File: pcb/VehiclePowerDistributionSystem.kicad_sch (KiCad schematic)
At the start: 28 parts, among them J1 B2B-XH-A, J2 B2B-XH-A, J3 B2B-XH-A, J4 B4B-XH-A, J5 B4B-XH-A, J6 B4B-XH-A, J7 B8B-XH-A, J8 FFC2B28-24-G, U1 TPS22810DRV, U2 D24V7F5, U3 D24V7F3, U7 TPS22810DRV

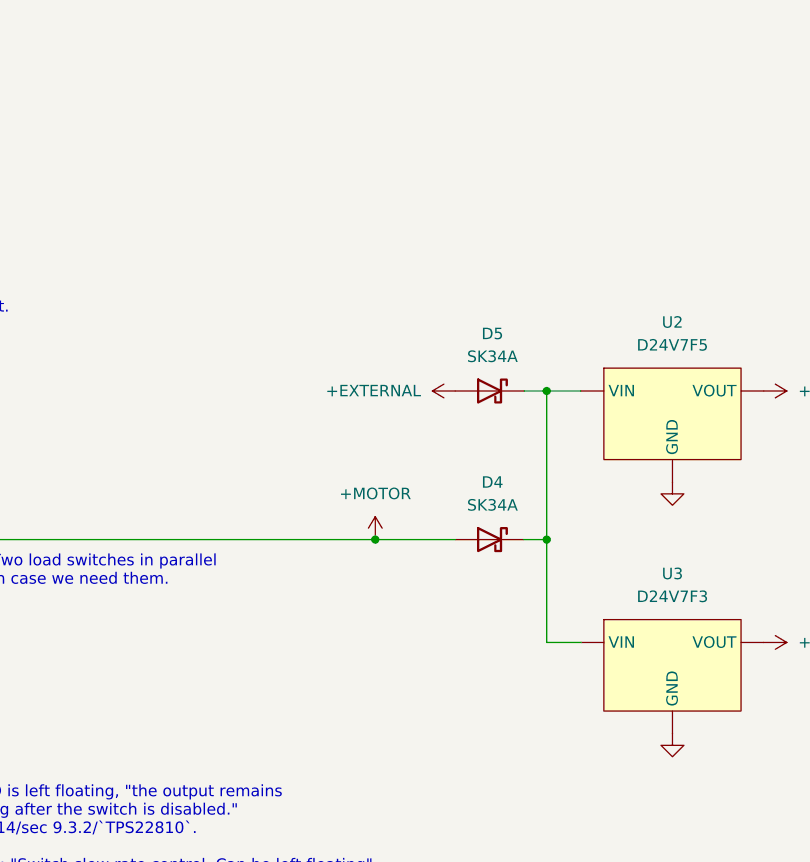
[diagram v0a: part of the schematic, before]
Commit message: Added LEDs for controlled battery and external power for `VehiclePowerDistributionSystem`.
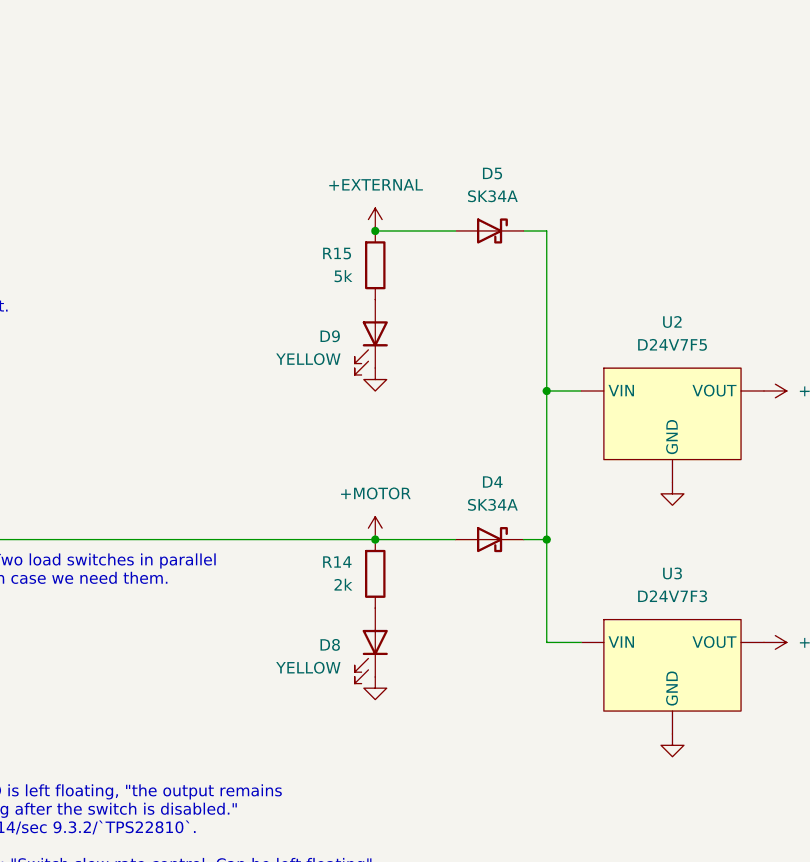
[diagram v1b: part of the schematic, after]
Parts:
- added D8, D9: YELLOW, LED_SMD:LED_1206_3216Metric_Pad1.42x1.75mm_HandSolder, symbol Device:LED
- added R14: 2k, Resistor_SMD:R_1206_3216Metric_Pad1.30x1.75mm_HandSolder, symbol Device:R
- added R15: 5k, Resistor_SMD:R_1206_3216Metric_Pad1.30x1.75mm_HandSolder, symbol Device:R
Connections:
- net +EXTERNAL: now also R15.2
- net +MOTOR: now also R14.2
- net GND: now also D8.1 (K), D9.1 (K)
- new net: D8.2 (A), R14.1
- new net: D9.2 (A), R15.1
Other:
- moved on the sheet: D5

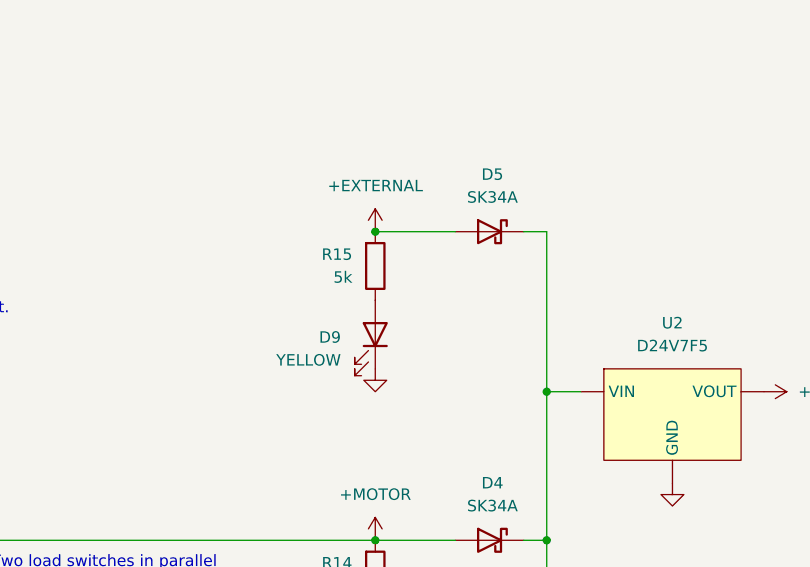
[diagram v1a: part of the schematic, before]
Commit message: Added more silkscreen text for `VehiclePowerDistributionSystem`.
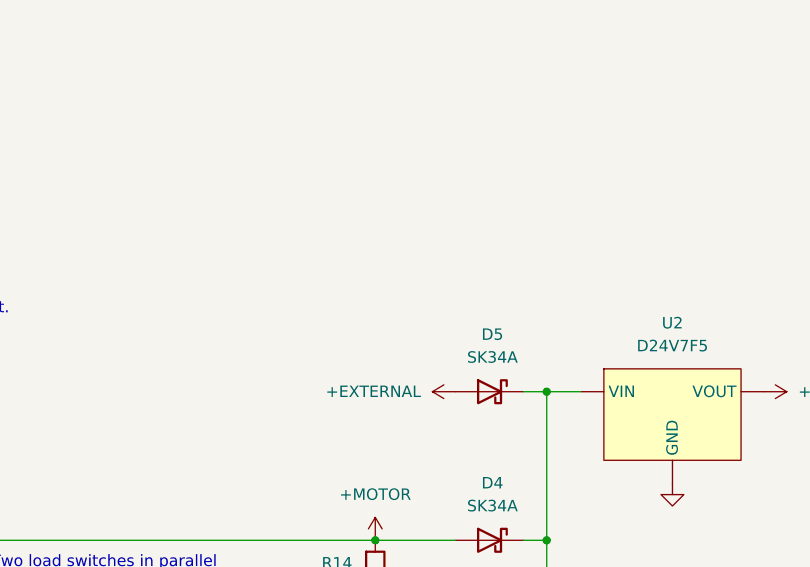
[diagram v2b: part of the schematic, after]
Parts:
- removed D9: YELLOW, LED_SMD:LED_1206_3216Metric_Pad1.42x1.75mm_HandSolder, symbol Device:LED
- removed R15: 5k, Resistor_SMD:R_1206_3216Metric_Pad1.30x1.75mm_HandSolder, symbol Device:R
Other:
- moved on the sheet: D5

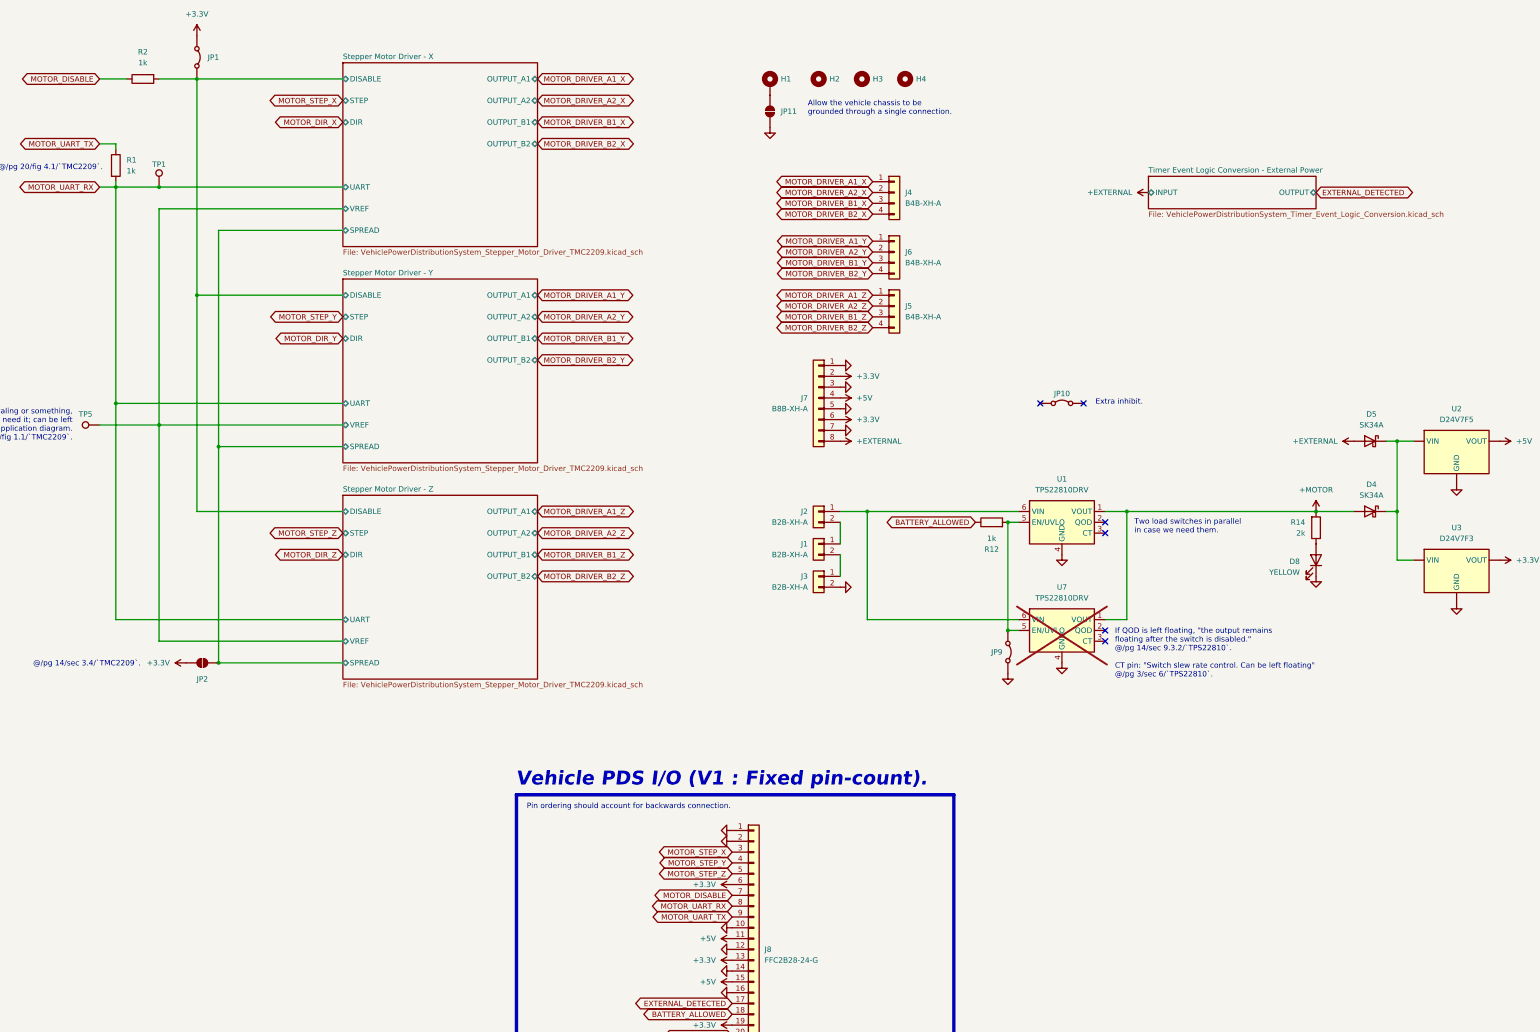
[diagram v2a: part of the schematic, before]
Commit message: Geographically reannotated `VehiclePowerDistributionSystem`.
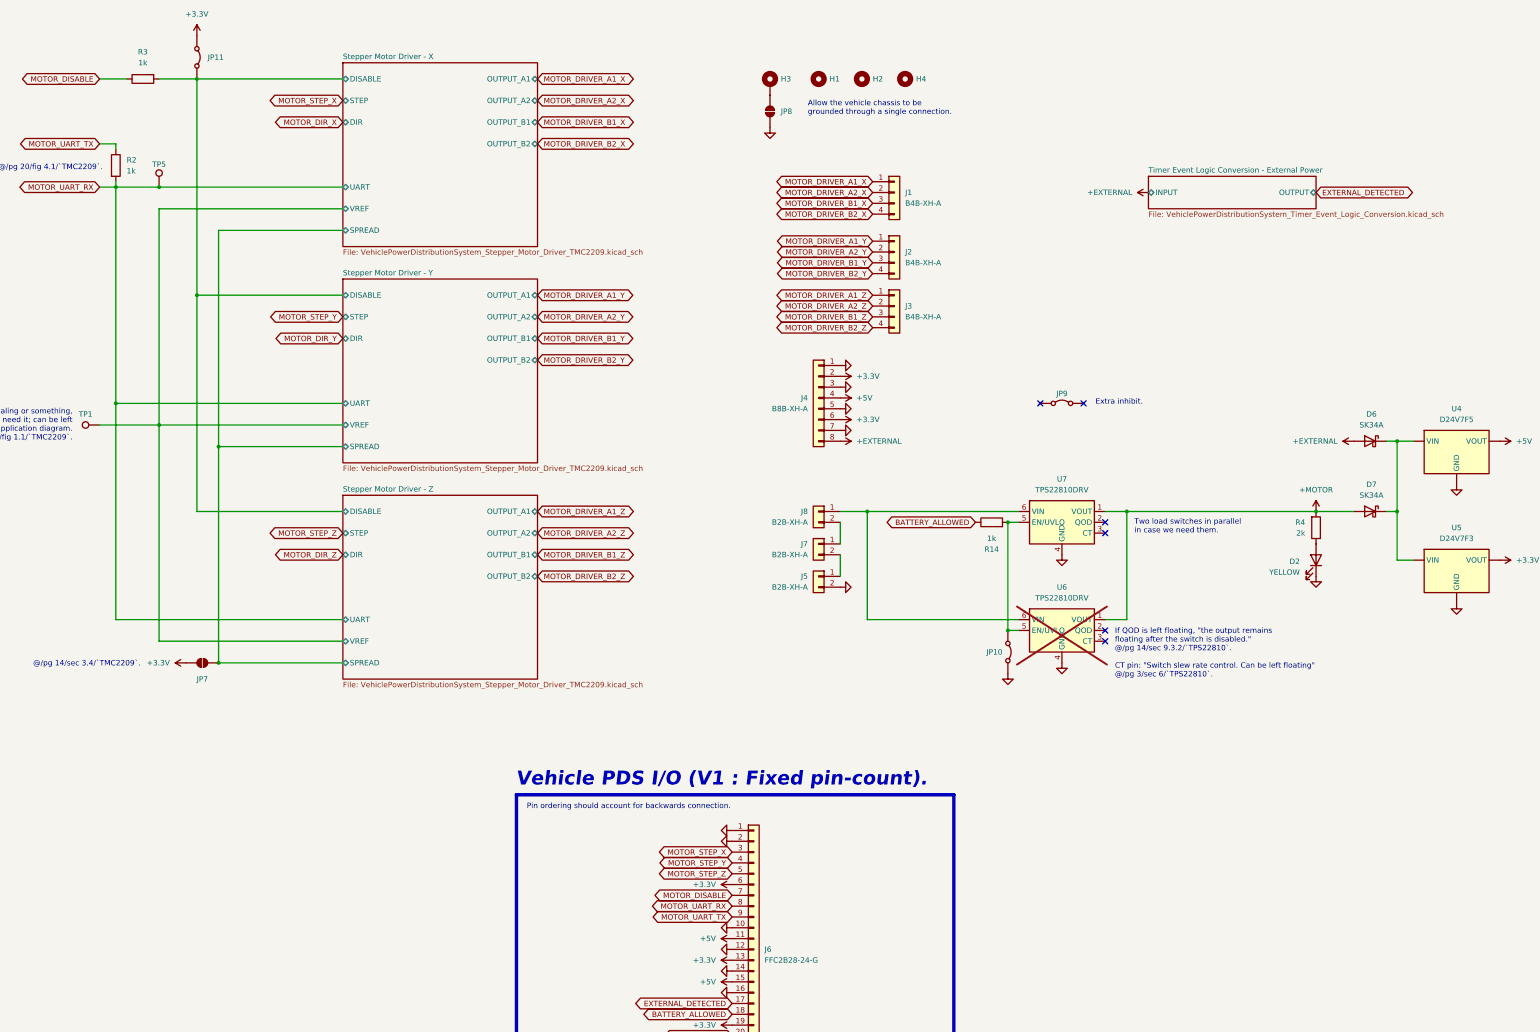
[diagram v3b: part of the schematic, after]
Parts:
- J6: renamed from J8; DigiKey (none) -> https://www.digikey.com/en/products/detail/gct/FFC2B28-24-G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
- renumbered D8 to D2, D5 to D6, D4 to D7, H2 to H1, H3 to H2, H1 to H3, J4 to J1, J6 to J2, J5 to J3, J7 to J4, J3 to J5, J1 to J7, J2 to J8, JP9 to JP10, JP1 to JP11, JP2 to JP7, JP11 to JP8, JP10 to JP9, R12 to R14, R1 to R2, R2 to R3, R14 to R4, TP5 to TP1, TP1 to TP5, U2 to U4, U3 to U5, U7 to U6, U1 to U7
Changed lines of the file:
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@@
 		(on_board yes)
 		(dnp no)
-		(property "Reference" "TP1"
+		(property "Reference" "TP5"
 			(at 81.28 58.166 0)
 			(effects
@@
 			(project "VehiclePowerDistributionSystem"
 				(path "/92a7a41c-8494-4e4b-ac2d-deb1f1cd8085"
-					(reference "TP1")
+					(reference "TP5")
 					(unit 1)
 				)
@@
 		(on_board yes)
 		(dnp no)
-		(property "Reference" "R12"
+		(property "Reference" "R14"
 			(at 276.86 148.59 90)
 			(effects
@@
 			(project "VehiclePowerDistributionSystem"
 				(path "/92a7a41c-8494-4e4b-ac2d-deb1f1cd8085"
-					(reference "R12")
+					(reference "R14")
 					(unit 1)
 				)
@@
 		(on_board yes)
 		(dnp no)
-		(property "Reference" "D8"
+		(property "Reference" "D2"
 			(at 349.25 151.4474 90)
 			(effects
@@
 			(project "VehiclePowerDistributionSystem"
 				(path "/92a7a41c-8494-4e4b-ac2d-deb1f1cd8085"
-					(reference "D8")
+					(reference "D2")
 					(unit 1)
 				)
@@
 		(dnp no)
 		(fields_autoplaced yes)
-		(property "Reference" "D5"
+		(property "Reference" "D6"
 			(at 366.0775 116.84 0)
 			(effects
@@
 			(project "VehiclePowerDistributionSystem"
 				(path "/92a7a41c-8494-4e4b-ac2d-deb1f1cd8085"
-					(reference "D5")
+					(reference "D6")
 					(unit 1)
 				)
@@
 		(on_board yes)
 		(dnp no)
-		(property "Reference" "J7"
+		(property "Reference" "J4"
 			(at 233.68 113.0299 0)
 			(effects
@@
 			(project "VehiclePowerDistributionSystem"
 				(path "/92a7a41c-8494-4e4b-ac2d-deb1f1cd8085"
-					(reference "J7")
+					(reference "J4")
 					(unit 1)
 				)
@@
 		(dnp no)
 		(fields_autoplaced yes)
-		(property "Reference" "H1"
+		(property "Reference" "H3"
 			(at 227.33 38.0999 0)
 			(effects
@@
 			(project "VehiclePowerDistributionSystem"
 				(path "/92a7a41c-8494-4e4b-ac2d-deb1f1cd8085"
-					(reference "H1")
+					(reference "H3")
 					(unit 1)
 				)
@@
 		(dnp no)
 		(fields_autoplaced yes)
-		(property "Reference" "J8"
+		(property "Reference" "J6"
 			(at 223.52 242.5699 0)
 			(effects
@@
 			)
 		)
+		(property "DigiKey" "https://www.digikey.com/en/products/detail/gct/FFC2B28-24-G/10656928"
+			(at 220.98 242.57 0)
+			(effects
+				(font
+					(size 1.27 1.27)
+				)
+				(hide yes)
+			)
+		)
 		(pin "17"
 		)
@@
 			(project ""
 				(path "/92a7a41c-8494-4e4b-ac2d-deb1f1cd8085"
-					(reference "J8")
+					(reference "J6")
 					(unit 1)
 				)
@@
 		(dnp no)
 		(fields_autoplaced yes)
-		(property "Reference" "JP11"
+		(property "Reference" "JP8"
 			(at 227.33 45.7199 90)
 			(effects
@@
 			(project "VehiclePowerDistributionSystem"
 				(path "/92a7a41c-8494-4e4b-ac2d-deb1f1cd8085"
-					(reference "JP11")
+					(reference "JP8")
 					(unit 1)
 				)
@@
 		(dnp no)
 		(fields_autoplaced yes)
-		(property "Reference" "JP9"
+		(property "Reference" "JP10"
 			(at 279.4 172.7199 90)
 			(effects
@@
 			(project "VehiclePowerDistributionSystem"
 				(path "/92a7a41c-8494-4e4b-ac2d-deb1f1cd8085"
-					(reference "JP9")
+					(reference "JP10")
 					(unit 1)
 				)
@@
 		(dnp no)
 		(fields_autoplaced yes)
-		(property "Reference" "J4"
+		(property "Reference" "J1"
 			(at 256.54 64.7699 0)
 			(effects
@@
 			(project ""
 				(path "/92a7a41c-8494-4e4b-ac2d-deb1f1cd8085"
-					(reference "J4")
+					(reference "J1")
 					(unit 1)
 				)
@@
 		(dnp no)
 		(fields_autoplaced yes)
-		(property "Reference" "J3"
+		(property "Reference" "J5"
 			(at 233.68 154.9399 0)
 			(effects
@@
 			(project "VehiclePowerDistributionSystem"
 				(path "/92a7a41c-8494-4e4b-ac2d-deb1f1cd8085"
-					(reference "J3")
+					(reference "J5")
 					(unit 1)
 				)
@@
 		(on_board yes)
 		(dnp no)
-		(property "Reference" "JP10"
+		(property "Reference" "JP9"
 			(at 293.37 112.014 0)
 			(effects
@@
 			(project "VehiclePowerDistributionSystem"
 				(path "/92a7a41c-8494-4e4b-ac2d-deb1f1cd8085"
-					(reference "JP10")
+					(reference "JP9")
 					(unit 1)
 				)
@@
 		(dnp no)
 		(fields_autoplaced yes)
-		(property "Reference" "U2"
+		(property "Reference" "U4"
 			(at 386.08 115.57 0)
 			(effects
@@
 			(project "VehiclePowerDistributionSystem"
 				(path "/92a7a41c-8494-4e4b-ac2d-deb1f1cd8085"
-					(reference "U2")
+					(reference "U4")
 					(unit 1)
 				)
@@
 		(dnp no)
 		(fields_autoplaced yes)
-		(property "Reference" "J1"
+		(property "Reference" "J7"
 			(at 233.68 147.3199 0)
 			(effects
@@
 			(project "VehiclePowerDistributionSystem"
 				(path "/92a7a41c-8494-4e4b-ac2d-deb1f1cd8085"
-					(reference "J1")
+					(reference "J7")
 					(unit 1)
 				)
@@
 		(on_board yes)
 		(dnp no)
-		(property "Reference" "H3"
+		(property "Reference" "H2"
 			(at 248.92 38.1 0)
 			(effects
@@
 			(project "VehiclePowerDistributionSystem"
 				(path "/92a7a41c-8494-4e4b-ac2d-deb1f1cd8085"
-					(reference "H3")
+					(reference "H2")
 					(unit 1)
 				)
@@
 		(dnp no)
 		(fields_autoplaced yes)
-		(property "Reference" "R1"
+		(property "Reference" "R2"
 			(at 73.66 57.1499 0)
 			(effects
@@
 			(project "VehiclePowerDistributionSystem"
 				(path "/92a7a41c-8494-4e4b-ac2d-deb1f1cd8085"
-					(reference "R1")
+					(reference "R2")
 					(unit 1)
 				)
@@
 		(dnp no)
 		(fields_autoplaced yes)
-		(property "Reference" "J2"
+		(property "Reference" "J8"
 			(at 233.68 139.6999 0)
 			(effects
@@
 			(project "VehiclePowerDistributionSystem"
 				(path "/92a7a41c-8494-4e4b-ac2d-deb1f1cd8085"
-					(reference "J2")
+					(reference "J8")
 					(unit 1)
 				)
@@
 		(dnp no)
 		(fields_autoplaced yes)
-		(property "Reference" "U1"
+		(property "Reference" "U7"
 			(at 293.37 132.08 0)
 			(effects
@@
 			(project "VehiclePowerDistributionSystem"
 				(path "/92a7a41c-8494-4e4b-ac2d-deb1f1cd8085"
-					(reference "U1")
+					(reference "U7")
 					(unit 1)
 				)
@@
 		(dnp no)
 		(fields_autoplaced yes)
-		(property "Reference" "TP5"
+		(property "Reference" "TP1"
 			(at 64.008 116.84 90)
 			(effects
@@
 			(project "VehiclePowerDistributionSystem"
 				(path "/92a7a41c-8494-4e4b-ac2d-deb1f1cd8085"
-					(reference "TP5")
+					(reference "TP1")
 					(unit 1)
 				)
@@
 		(on_board yes)
 		(dnp no)
-		(property "Reference" "JP2"
+		(property "Reference" "JP7"
 			(at 91.44 179.07 0)
 			(effects
@@
 			(project "VehiclePowerDistributionSystem"
 				(path "/92a7a41c-8494-4e4b-ac2d-deb1f1cd8085"
-					(reference "JP2")
+					(reference "JP7")
 					(unit 1)
 				)
@@
 		(dnp no)
 		(fields_autoplaced yes)
-		(property "Reference" "U3"
+		(property "Reference" "U5"
 			(at 386.08 143.51 0)
 			(effects
@@
 			(project "VehiclePowerDistributionSystem"
 				(path "/92a7a41c-8494-4e4b-ac2d-deb1f1cd8085"
-					(reference "U3")
+					(reference "U5")
 					(unit 1)
 				)
@@
 		(on_board yes)
 		(dnp no)
-		(property "Reference" "R14"
+		(property "Reference" "R4"
 			(at 350.52 142.2399 0)
 			(effects
@@
 			(project "VehiclePowerDistributionSystem"
 				(path "/92a7a41c-8494-4e4b-ac2d-deb1f1cd8085"
-					(reference "R14")
+					(reference "R4")
 					(unit 1)
 				)
@@
 		(on_board yes)
 		(dnp no)
-		(property "Reference" "H2"
+		(property "Reference" "H1"
 			(at 238.76 38.1 0)
 			(effects
@@
 			(project "VehiclePowerDistributionSystem"
 				(path "/92a7a41c-8494-4e4b-ac2d-deb1f1cd8085"
-					(reference "H2")
+					(reference "H1")
 					(unit 1)
 				)
@@
 		(dnp no)
 		(fields_autoplaced yes)
-		(property "Reference" "J6"
+		(property "Reference" "J2"
 			(at 256.54 78.7399 0)
 			(effects
@@
 			(project "VehiclePowerDistributionSystem"
 				(path "/92a7a41c-8494-4e4b-ac2d-deb1f1cd8085"
-					(reference "J6")
+					(reference "J2")
 					(unit 1)
 				)
@@
 		(dnp no)
 		(fields_autoplaced yes)
-		(property "Reference" "R2"
+		(property "Reference" "R3"
 			(at 77.47 31.75 90)
 			(effects
@@
 			(project "VehiclePowerDistributionSystem"
 				(path "/92a7a41c-8494-4e4b-ac2d-deb1f1cd8085"
-					(reference "R2")
+					(reference "R3")
 					(unit 1)
 				)
@@
 		(dnp no)
 		(fields_autoplaced yes)
-		(property "Reference" "JP1"
+		(property "Reference" "JP11"
 			(at 92.71 33.0199 90)
 			(effects
@@
 			(project "VehiclePowerDistributionSystem"
 				(path "/92a7a41c-8494-4e4b-ac2d-deb1f1cd8085"
-					(reference "JP1")
+					(reference "JP11")
 					(unit 1)
 				)
@@
 		(dnp no)
 		(fields_autoplaced yes)
-		(property "Reference" "J5"
+		(property "Reference" "J3"
 			(at 256.54 91.4399 0)
 			(effects
@@
 			(project "VehiclePowerDistributionSystem"
 				(path "/92a7a41c-8494-4e4b-ac2d-deb1f1cd8085"
-					(reference "J5")
+					(reference "J3")
 					(unit 1)
 				)
@@
 		(dnp no)
 		(fields_autoplaced yes)
-		(property "Reference" "D4"
+		(property "Reference" "D7"
 			(at 366.0775 133.35 0)
 			(effects
@@
 			(project ""
 				(path "/92a7a41c-8494-4e4b-ac2d-deb1f1cd8085"
-					(reference "D4")
+					(reference "D7")
 					(unit 1)
 				)
@@
 		(dnp yes)
 		(fields_autoplaced yes)
-		(property "Reference" "U7"
+		(property "Reference" "U6"
 			(at 293.37 157.48 0)
 			(effects
@@
 			(project "VehiclePowerDistributionSystem"
 				(path "/92a7a41c-8494-4e4b-ac2d-deb1f1cd8085"
-					(reference "U7")
+					(reference "U6")
 					(unit 1)
 				)
